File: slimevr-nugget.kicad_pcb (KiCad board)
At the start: 4 copper layers, 24 x 17.5 mm, 54 parts, among them U1 nRF52840-QFXX, U2 BQ24075RGT, U3 XC6220B331MR, U4 ICM-45686, U5 1532H, U6 QMC6309, Y1 32MHz

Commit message: Revision 2
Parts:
- removed D1: ORANGE, LED_SMD:LED_0402_1005Metric
- removed D2: LED, LED_SMD:LED_0402_1005Metric
- removed U2: BQ24075RGT, Package_DFN_QFN:VQFN-16-1EP_3x3mm_P0.5mm_EP1.6x1.6mm
- added R12: 10k, Resistor_SMD:R_0402_1005Metric, F.Cu at (95.3, 140.1)
- added TP5: GND, TestPoint:TestPoint_Pad_D1.0mm, F.Cu at (101.4, 139.7)
- added TP6: BAT+, TestPoint:TestPoint_Pad_D1.0mm, F.Cu at (98.2, 139.7)
- added TP7: CHRG, TestPoint:TestPoint_Pad_D1.5mm, B.Cu at (94.4, 140.7)
- added U7: BQ24073RGT, Package_DFN_QFN:VQFN-16-1EP_3x3mm_P0.5mm_EP1.6x1.6mm, F.Cu at (98.0, 143.7)
- C24: value 1.0uF -> 100nF
- R4: value 10M -> 10k
- U4: value ICM-45686 -> LSM6DSV
- moved R4 11.2 mm to (101.2, 141.7), turned to 180 degrees
- moved R2 3.30 mm to (95.3, 142.0), turned to 180 degrees
- moved R11 2.03 mm to (95.3, 141.0), turned to 180 degrees
- moved TP1 1.84 mm to (94.4, 143.3)
- moved TP3 1.84 mm to (94.4, 148.3)
- moved TP4 1.84 mm to (94.4, 150.9)
- moved TP2 1.84 mm to (94.4, 145.8)
- moved C19 1.28 mm to (94.5, 147.3)
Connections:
- R11 pad 1: Net-(D2-K) -> GND
- R11 pad 2: GND -> Net-(U7-ILIM)
- R2 pad 1: Net-(D1-A) -> CHG
- R2 pad 2: VDDH -> VBUS
- R3 pad 1: GND -> Net-(R3-Pad1)
- R4 pad 1: VDDH -> GND
- R4 pad 2: PWRPIN -> Net-(R3-Pad1)
- U1 pad 13: PWRPIN -> unconnected-(U1-P0.13-Pad13)
- U1 pad 23: unconnected-(U1-P0.24-Pad23) -> INT1
- U3 pad 3: PWRPIN -> VDDH
- U4 pad 7: unconnected-(U4-GND-Pad7) -> GND
- U4 pad 9: CLK -> unconnected-(U4-INT2-Pad9)
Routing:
- net GND: track 58.0 -> 108.0 mm, vias 14 -> 37
- net CLK: track 32.2 -> 7.34 mm, vias 3 -> 2
- net VDD: track 42.2 -> 59.2 mm, vias 8 -> 10
- net INT1: track 0.00 -> 17.0 mm, vias 0 -> 2
- net Net-(U7-ILIM): track 0.00 -> 8.56 mm, vias 0 -> 2
- net Net-(U1-DEC4): track 20.8 -> 13.3 mm
- net Net-(R3-Pad1): track 0.00 -> 6.71 mm, vias 0 -> 2
- net BAT+: track 0.00 -> 6.63 mm, vias 0 -> 3
- net VDDH: track 24.0 -> 18.2 mm
- net VBUS: track 13.4 -> 9.33 mm, vias 1 -> 2
- net CHG: track 0.00 -> 4.03 mm, vias 0 -> 1
- net Net-(D1-A): track 3.63 -> 0.00 mm
- net SWC: track 22.8 -> 20.5 mm
- net PWRPIN: track 1.27 -> 0.00 mm
- net Net-(D1-K): track 1.24 -> 0.00 mm
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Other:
- outline, holes or cut-outs redrawn
- board text added: "0"
- board text added: "B+"
- board text added: "SWD SWC GND +5V CHG"
- board text added: "info's nugget"
- board text added: "owo"
- board text added: "rev.2"
- board text added: "rm?"
- board text removed: "SWD SWC GND +5V"

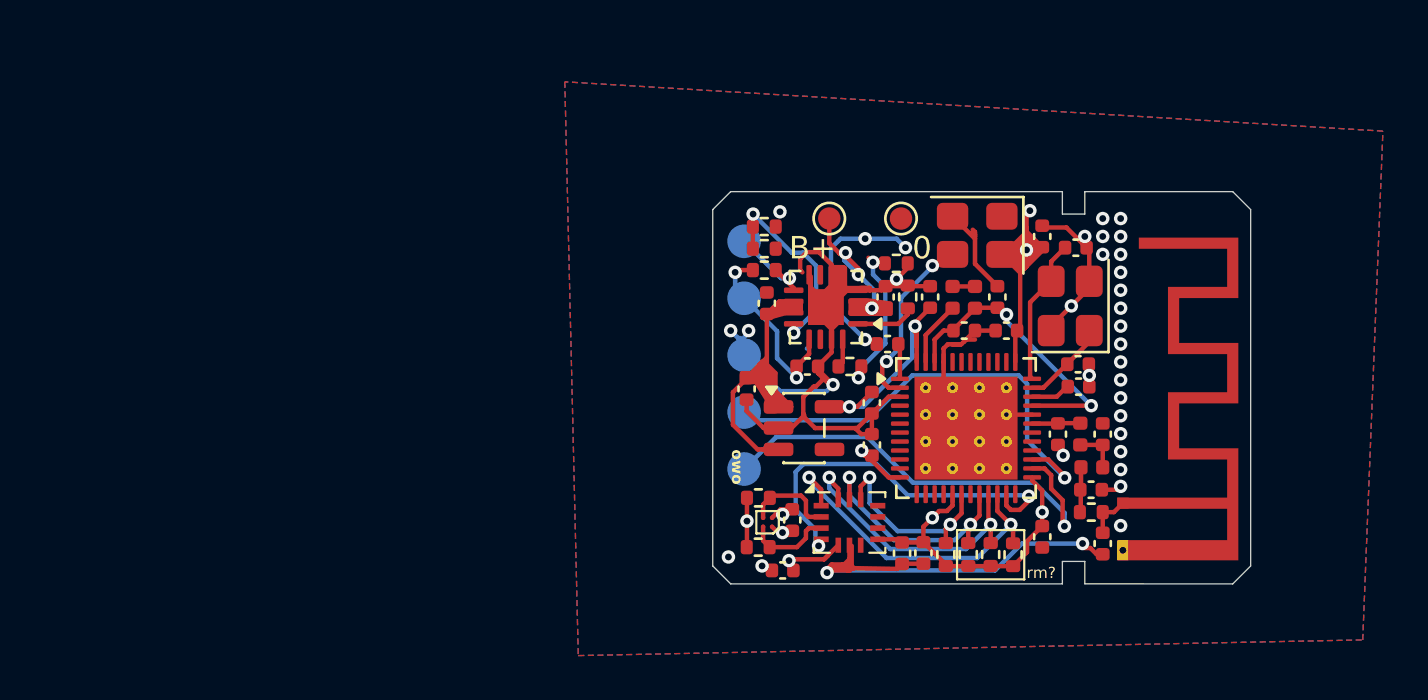
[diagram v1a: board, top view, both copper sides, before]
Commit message: Turn off system by pulling down CE of LDO while charging
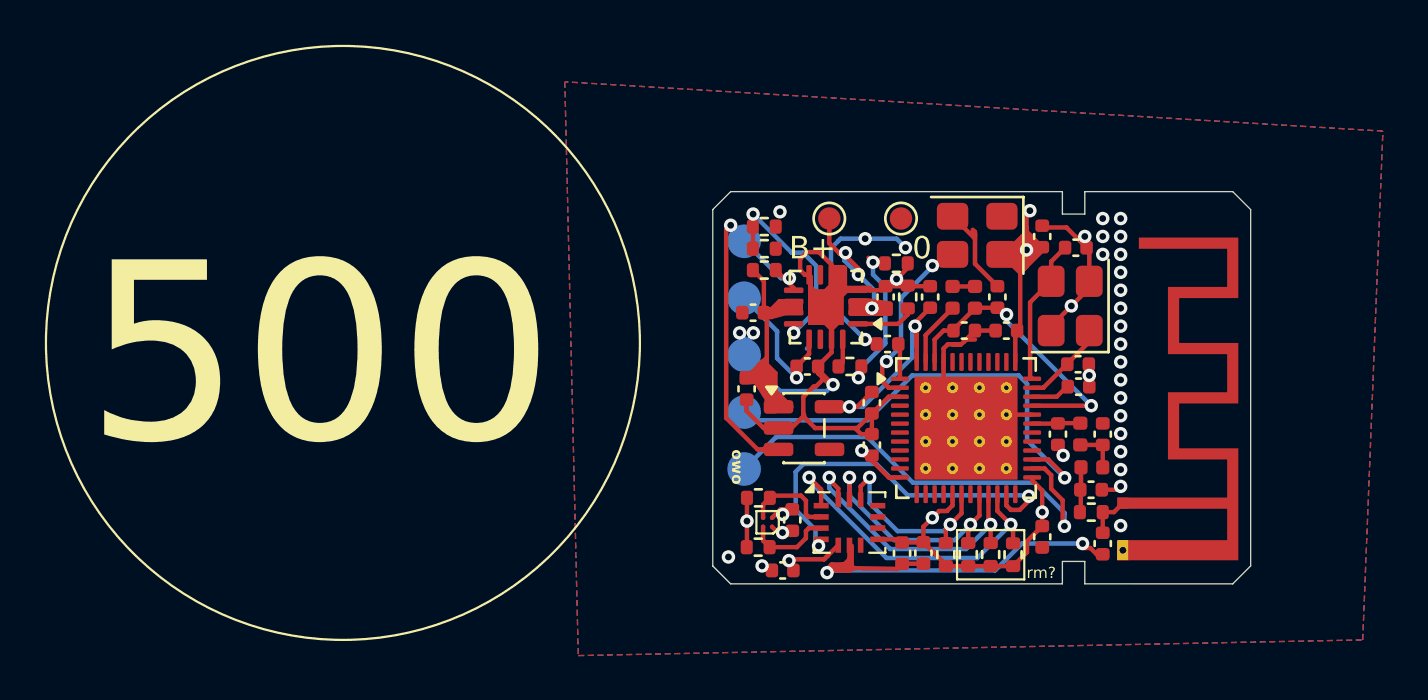
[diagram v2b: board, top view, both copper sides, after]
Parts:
- moved C18 0.74 mm to (94.8, 143.9), turned to 0 degrees
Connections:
- R2 pad 2: VBUS -> VDDH
- U3 pad 3: VDDH -> CHG
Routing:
- net CHG: track 4.03 -> 16.5 mm, vias 1 -> 2
- net VDDH: track 18.2 -> 15.3 mm
- net GND: track 108.0 -> 109.6 mm
- net VBUS: track 9.33 -> 7.74 mm, vias 2 -> 1
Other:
- board text added: "500"

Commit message: Final production version
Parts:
- added D1: LED, LED_SMD:LED_0402_1005Metric, F.Cu at (97.2, 140.8)
- added D2: LED, LED_SMD:LED_0402_1005Metric, F.Cu at (97.2, 139.8)
- added R13: 10k, Resistor_SMD:R_0402_1005Metric, F.Cu at (94.8, 143.0)
- added R14: 1k, Resistor_SMD:R_0402_1005Metric, F.Cu at (101.9, 153.2)
- R2: value 10k -> 1k
- moved TP6 1.10 mm to (99.3, 139.6)
- moved C18 0.10 mm to (94.8, 144.0)
- moved TP5 0.10 mm to (101.4, 139.6)
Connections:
- R2 pad 1: CHG -> Net-(D1-A)
- U1 pad 13: unconnected-(U1-P0.13-Pad13) -> Net-(U1-P0.13)
- U7 pad 9: CHG -> Net-(D1-K)
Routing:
- net Net-(D2-A): track 0.00 -> 29.9 mm, vias 0 -> 2
- net CHG: track 16.5 -> 12.9 mm, vias 2 -> 1
- net GND: track 109.6 -> 106.1 mm, vias 37 -> 36
- net Net-(D1-K): track 0.00 -> 2.82 mm
- net Net-(D1-A): track 0.00 -> 1.67 mm
- net Net-(U1-P0.13): track 0.00 -> 1.29 mm
- net Net-(U7-ILIM): track 8.56 -> 7.44 mm
- net BAT+: track 6.63 -> 6.10 mm
- net VDD: track 59.2 -> 59.1 mm, vias 10 -> 9

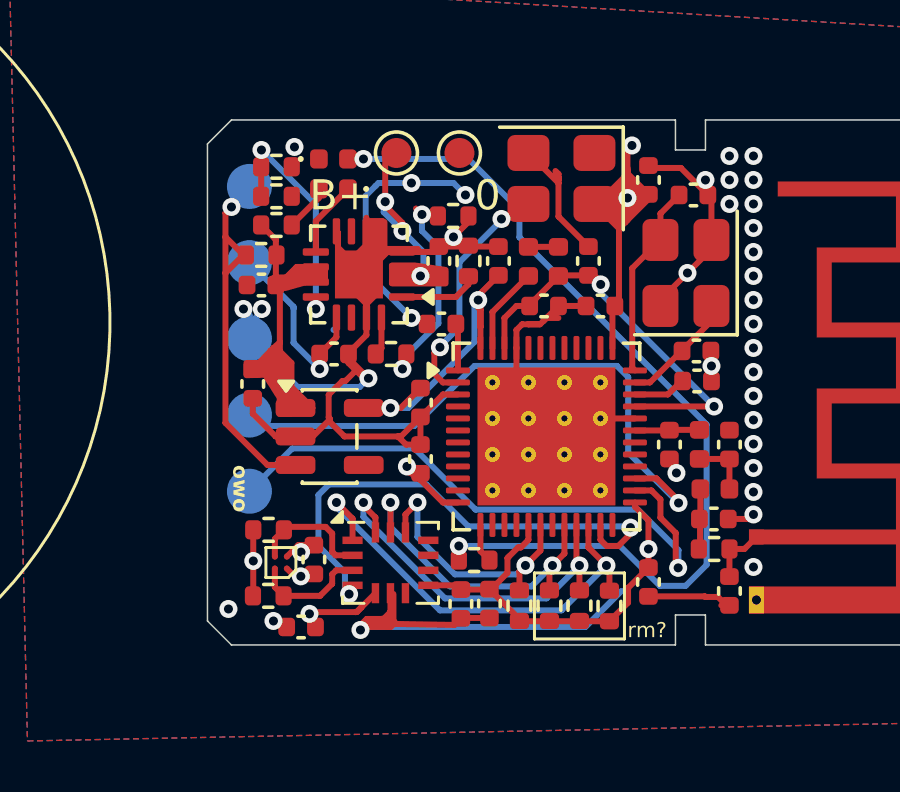
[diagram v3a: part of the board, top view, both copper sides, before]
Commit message: Add 1:1 battery sensing circuit
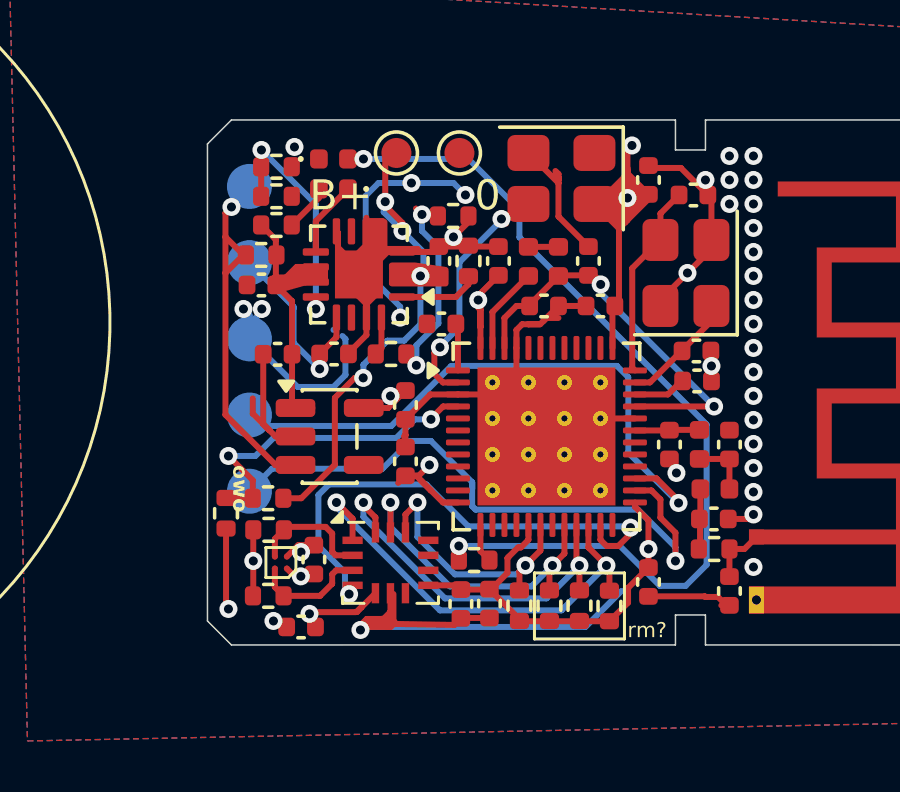
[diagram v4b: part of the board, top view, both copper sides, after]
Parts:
- added R15: 100k, Resistor_SMD:R_0402_1005Metric, F.Cu at (93.6, 151.6)
- added R16: 100k, Resistor_SMD:R_0402_1005Metric, F.Cu at (95.0, 151.1)
- R13: value 10k -> 100k
- moved C19 1.29 mm to (95.3, 146.3), turned to 0 degrees
- moved C20 0.51 mm to (99.6, 148.0)
- moved C12 0.51 mm to (99.6, 149.9)
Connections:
- U1 pad 4: unconnected-(U1-P0.04-Pad4) -> BSENSE
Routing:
- net BSENSE: track 0.00 -> 11.0 mm, vias 0 -> 2
- net BAT+: track 6.10 -> 16.2 mm, vias 3 -> 4
- net VDDH: track 15.3 -> 9.34 mm
- net VDD: track 59.1 -> 55.1 mm
- net GND: track 106.1 -> 106.0 mm, vias 36 -> 35

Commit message: Change to nRF52833, swap antenna matching circuit to IC
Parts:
- removed C15: 1.0uF, Capacitor_SMD:C_0402_1005Metric
- removed C23, C4: TODO, Capacitor_SMD:C_0402_1005Metric
- removed C5: 1.0pF, Capacitor_SMD:C_0402_1005Metric
- removed C6: 1.2pF, Capacitor_SMD:C_0402_1005Metric
- removed C9: 47nF, Capacitor_SMD:C_0402_1005Metric
- removed L1: 4.7nH, Inductor_SMD:L_0402_1005Metric
- removed L2: 2.2nH, Inductor_SMD:L_0402_1005Metric
- removed L3: 10uH, Inductor_SMD:L_0402_1005Metric
- removed L4: 15nH, Inductor_SMD:L_0402_1005Metric
- removed L5: TODO, Resistor_SMD:R_0402_1005Metric
- removed U1: nRF52840-QFXX, Package_DFN_QFN:QFN-48-1EP_6x6mm_P0.4mm_EP4.6x4.6mm_ThermalVias
- added FL1: 2450FM07B0037, 2450FM07B0037:2450FM07B0037, F.Cu at (108.2, 149.2)
- added U2: nRF52833_QDxx, Package_DFN_QFN:QFN-40-1EP_5x5mm_P0.4mm_EP3.6x3.6mm, F.Cu at (103.9, 148.6)
- C11: value 100nF -> 4.7uF
- C14: value 100nF -> 1.0uF
- moved R15 13.9 mm to (104.7, 143.2), turned to -90 degrees
- moved R16 11.7 mm to (103.7, 143.2), turned to 90 degrees
- moved R14 10.6 mm to (105.6, 143.2), turned to -90 degrees
- moved C8 3.33 mm to (102.7, 144.6)
- moved C1 1.71 mm to (107.7, 146.7), turned to -90 degrees
- moved C13 0.30 mm to (106.1, 145.0)
- moved C7 0.16 mm to (109.2, 147.1)
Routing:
- net Net-(D2-A): track 29.9 -> 10.2 mm
- net BSENSE: track 11.0 -> 3.45 mm, vias 2 -> 0
- net SWD: track 20.7 -> 14.9 mm
- net SWC: track 20.5 -> 15.0 mm
- net INT1: track 17.0 -> 11.5 mm, vias 2 -> 4
- net BAT+: track 16.2 -> 11.7 mm, vias 4 -> 3
- net CLK: track 7.34 -> 11.3 mm
- net Net-(U1-DCC): track 2.90 -> 0.00 mm
- net Net-(R3-Pad1): track 6.40 -> 8.87 mm
- net Net-(U2-AIN6/P0.30): track 1.29 -> 3.63 mm
- net Net-(U1-ANT): track 2.17 -> 0.00 mm
- net Net-(C4-Pad2): track 2.02 -> 0.00 mm
- net Net-(C6-Pad2): track 2.00 -> 0.00 mm
- net SDA: track 12.7 -> 14.4 mm
- net GND: track 106.0 -> 107.5 mm, vias 35 -> 44
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
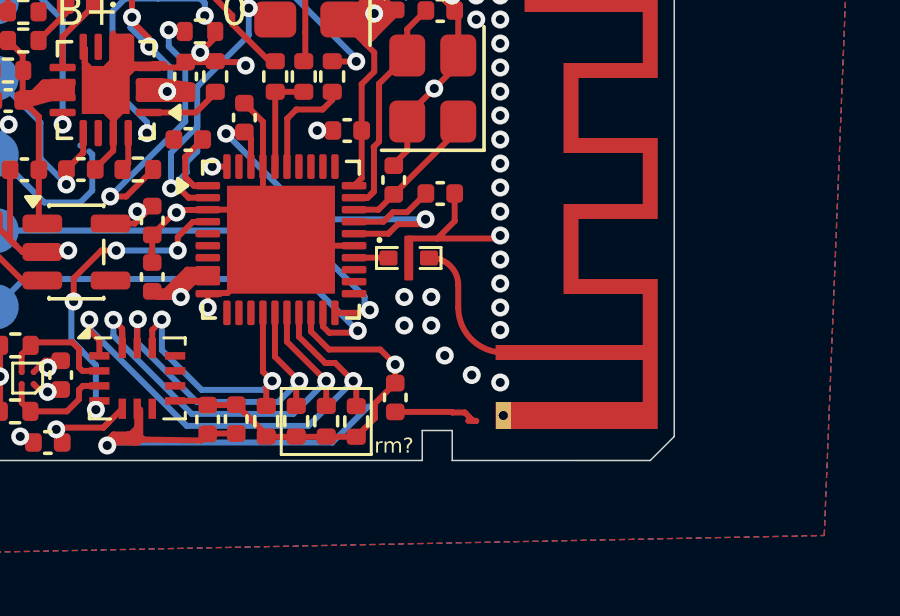
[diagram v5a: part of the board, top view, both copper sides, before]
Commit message: Impedance match 2.4GHz trace
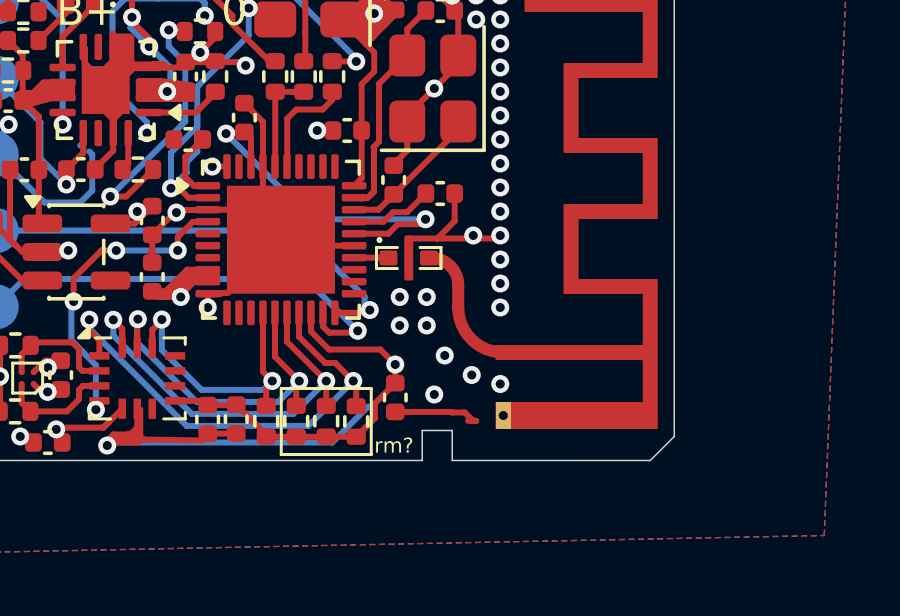
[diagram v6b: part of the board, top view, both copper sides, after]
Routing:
- net GND: track 107.5 -> 107.3 mm, vias 44 -> 45
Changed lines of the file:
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@@
 		(end 109.8 150.15)
 		(stroke
-			(width 0.2)
-			(type default)
+			(width 0.4)
+			(type solid)
 		)
 		(layer "F.Cu")
@@
 		(end 109.8 150.9)
 		(stroke
-			(width 0.2)
-			(type default)
+			(width 0.4)
+			(type solid)
 		)
 		(layer "F.Cu")
@@
 	)
 	(segment
-		(start 111.2 151.649998)
-		(end 111.049998 151.8)
-		(width 0.2)
-		(layer "F.Cu")
-		(net "GND")
-	)
-	(segment
 		(start 100.406114 147.736)
 		(end 100.344 147.736)
@@
 	)
 	(via
+		(at 110.3 148.5)
+		(size 0.6)
+		(drill 0.3)
+		(layers "F.Cu" "B.Cu")
+		(net "GND")
+	)
+	(via
 		(at 111.2 139.7)
 		(size 0.6)
@@
 	)
 	(via
-		(at 108 150.55)
+		(at 107.85 150.55)
 		(size 0.6)
 		(drill 0.3)
@@
 	)
 	(via
-		(at 108 151.5)
+		(at 107.85 151.5)
 		(size 0.6)
 		(drill 0.3)
@@
 	)
 	(via
-		(at 108.9 151.5)
+		(at 108.75 151.5)
 		(size 0.6)
 		(drill 0.3)
@@
 	)
 	(via
-		(at 111.2 153.4)
+		(at 111.2 153.45)
 		(size 0.6)
 		(drill 0.3)
@@
 	)
 	(via
-		(at 111.2 151.649998)
-		(size 0.6)
-		(drill 0.3)
-		(layers "F.Cu" "B.Cu")
-		(capping no)
-		(covering
-			(front no)
-			(back no)
-		)
-		(plugging
-			(front no)
-			(back no)
-		)
-		(filling no)
-		(net "GND")
-	)
-	(via
 		(at 111.2 146.9)
 		(size 0.6)
@@
 	)
 	(via
+		(at 109 153.8)
+		(size 0.6)
+		(drill 0.3)
+		(layers "F.Cu" "B.Cu")
+		(free yes)
+		(net "GND")
+	)
+	(via
 		(at 95.2 155.2)
 		(size 0.6)
@@
 	)
 	(via
-		(at 108.9 150.55)
+		(at 108.75 150.55)
 		(size 0.6)
 		(drill 0.3)
@@
 	)
 	(segment
+		(start 107.465 149.24)
+		(end 107.475 149.25)
+		(width 0.2)
+		(layer "F.Cu")
+		(net "Net-(FL1-IN)")
+	)
+	(segment
+		(start 106.3275 149.24)
+		(end 107.465 149.24)
+		(width 0.2)
+		(layer "F.Cu")
+		(net "Net-(FL1-IN)")
+	)
+	(segment
 		(start 102.15 145.05)
 		(end 102.67 145.05)
@@
 	)
 	(segment
+		(start 109.8 150.15)
+		(end 109.8 150.9)
+		(width 0.4)
+		(layer "F.Cu")
+		(net "Net-(AE1-A)")
+	)
+	(segment
 		(start 97.1585 152.2835)
 		(end 96.9375 152.0625)
@@
 		(net "CHG")
 	)
-	(segment
-		(start 109.8 150.15)
-		(end 109.8 150.9)
-		(width 0.2)
-		(layer "F.Cu")
-		(net "Net-(AE1-A)")
-	)
-	(segment
-		(start 107.465 149.24)
-		(end 107.475 149.25)
-		(width 0.2)
-		(layer "F.Cu")
-		(net "Net-(FL1-IN)")
-	)
-	(segment
-		(start 106.3275 149.24)
-		(end 107.465 149.24)
-		(width 0.2)
-		(layer "F.Cu")
-		(net "Net-(FL1-IN)")
-	)
 	(zone
